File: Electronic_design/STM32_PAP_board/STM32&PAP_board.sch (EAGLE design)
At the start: 21 parts

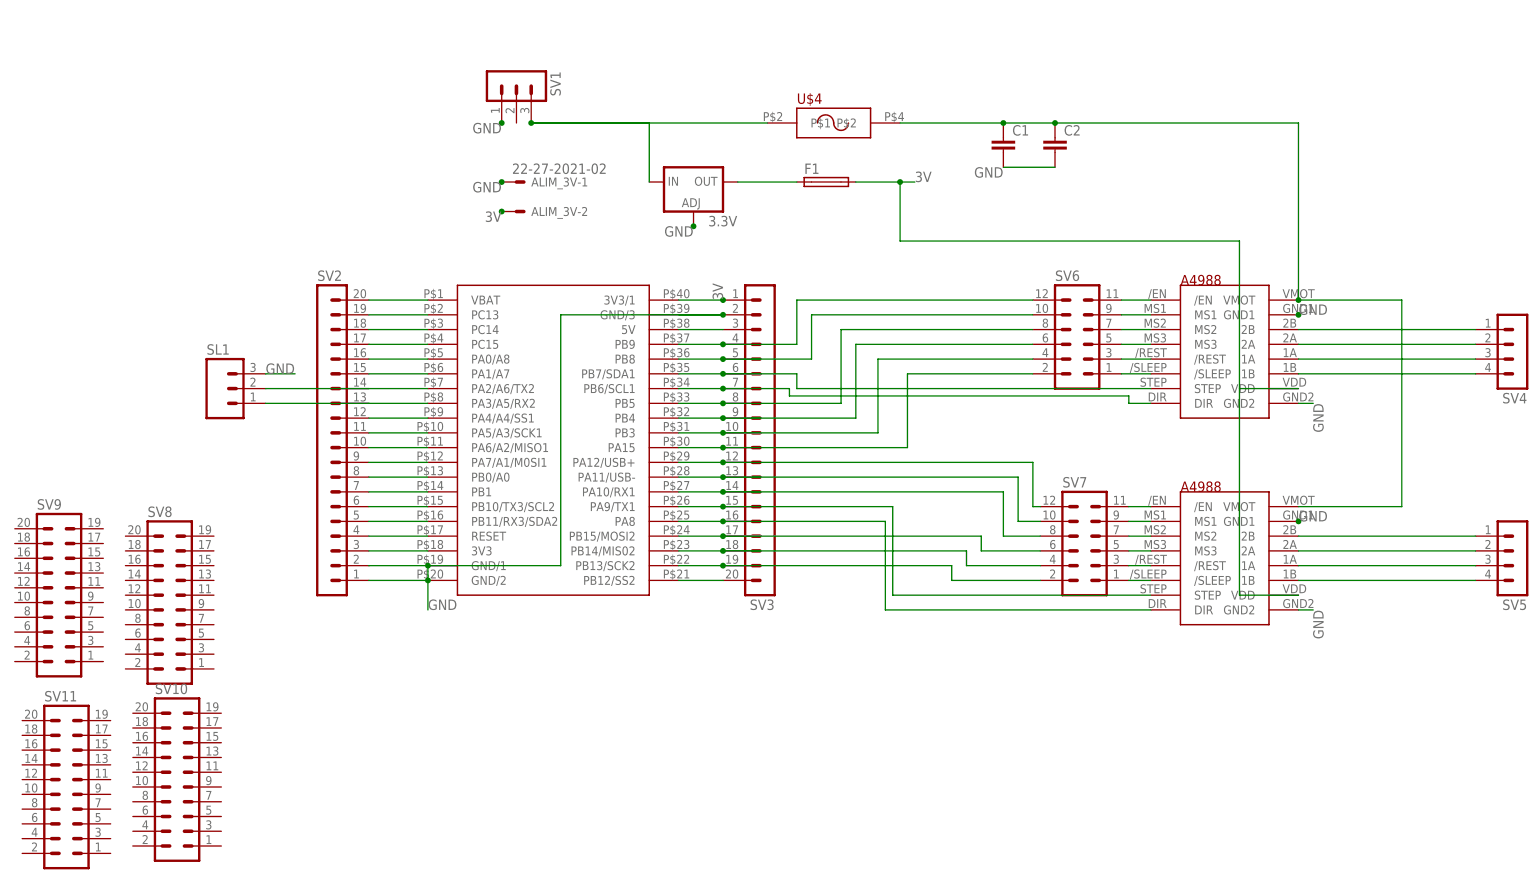
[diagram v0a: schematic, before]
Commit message: modification regulateur 3V3
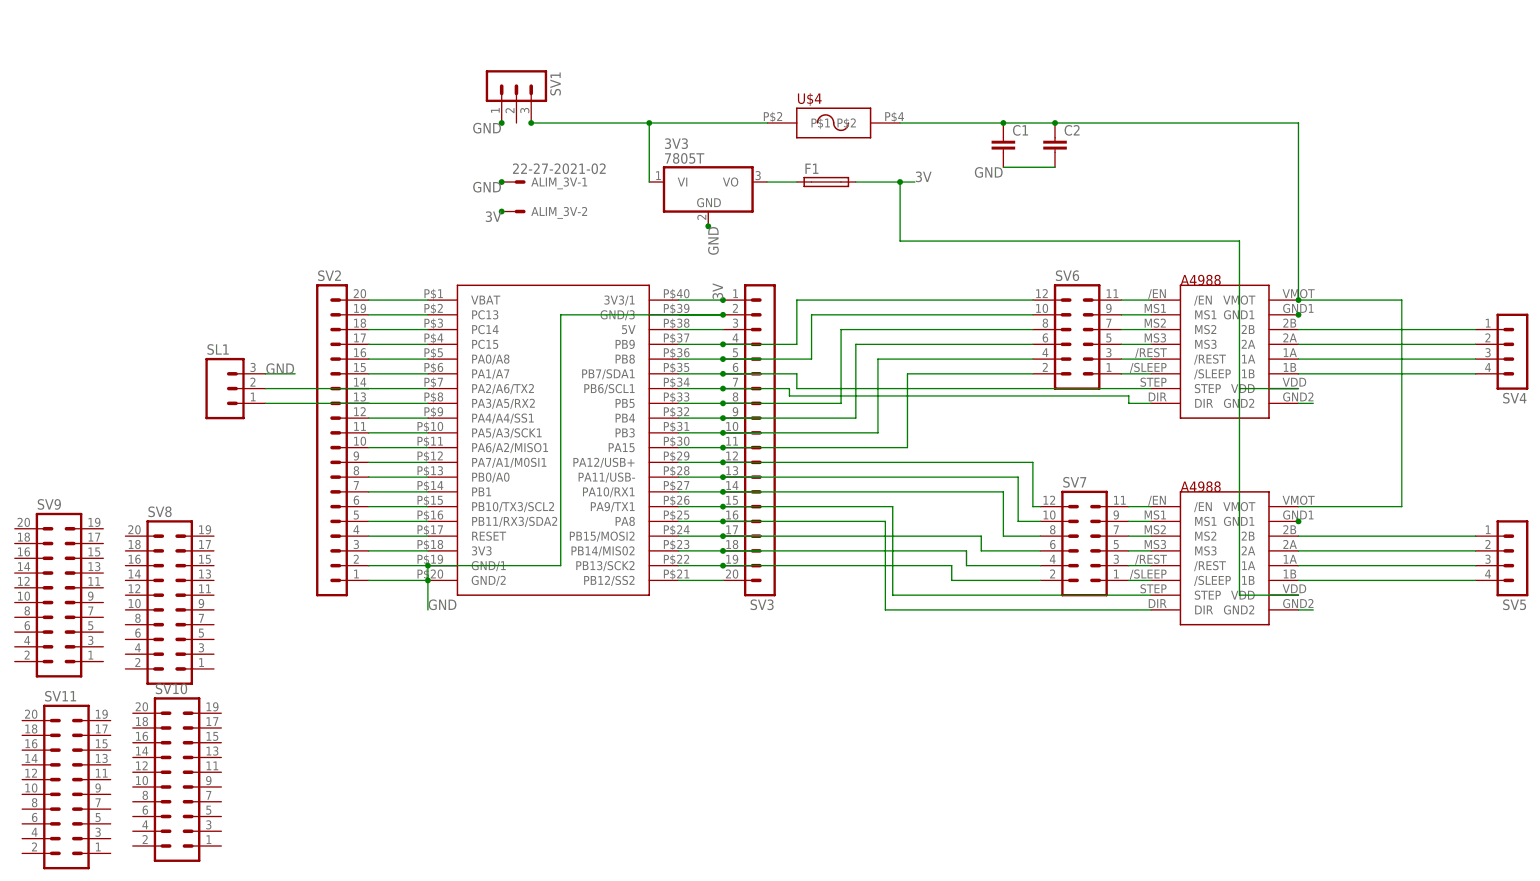
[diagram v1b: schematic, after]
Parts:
- removed 3.3V: (no value), v-reg:LM138-TS
- added 3V3: 7805T, linear:7805T
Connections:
- net GND: now also 3V3.GND; no longer 3.3V.ADJ
- net N$41: now also 3V3.VO; no longer 3.3V.OUT
- net N$42: now also 3V3.VI; no longer 3.3V.IN
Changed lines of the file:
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@@
 <part name="SV2" library="con-lstb" deviceset="MA20-1" device=""/>
 <part name="SV3" library="con-lstb" deviceset="MA20-1" device=""/>
-<part name="3.3V" library="v-reg" deviceset="LM138-TS" device=""/>
 <part name="SV4" library="con-lstb" deviceset="MA04-1" device=""/>
 <part name="SV5" library="con-lstb" deviceset="MA04-1" device=""/>
@@
 <part name="F1" library="fuse" deviceset="TR5" device=""/>
 <part name="SL1" library="con-amp-quick" deviceset="MA03" device=""/>
+<part name="3V3" library="linear" library_urn="urn:adsk.eagle:library:262" deviceset="78*" device="T" package3d_urn="urn:adsk.eagle:package:16414/1" technology="05"/>
 </parts>
 <sheets>
@@
 <instance part="SV2" gate="1" x="-81.28" y="5.08"/>
 <instance part="SV3" gate="1" x="-5.08" y="7.62" rot="R180"/>
-<instance part="3.3V" gate="G$1" x="-17.78" y="50.8"/>
 <instance part="SV4" gate="1" x="124.46" y="20.32" rot="R180"/>
 <instance part="SV5" gate="1" x="124.46" y="-15.24" rot="R180"/>
@@
 <instance part="F1" gate="1" x="5.08" y="50.8"/>
 <instance part="SL1" gate="G$1" x="-99.06" y="15.24"/>
+<instance part="3V3" gate="A1" x="-15.24" y="50.8"/>
 </instances>
 <busses>
@@
 </net>
 <net name="GND" class="0">
-<segment>
-<pinref part="3.3V" gate="G$1" pin="ADJ"/>
-<junction x="-17.78" y="43.18"/>
-<label x="-17.78" y="43.18" size="1.778" layer="95" rot="R180"/>
-<label x="86.36" y="27.94" size="1.778" layer="95"/>
-<label x="86.36" y="-7.62" size="1.778" layer="95"/>
-<label x="88.9" y="12.7" size="1.778" layer="95" rot="R270"/>
-<label x="88.9" y="-22.86" size="1.778" layer="95" rot="R270"/>
-</segment>
 <segment>
 <pinref part="U$3" gate="G$1" pin="GND/1"/>
@@
 <label x="-91.44" y="17.78" size="1.778" layer="95"/>
 </segment>
+<segment>
+<pinref part="3V3" gate="A1" pin="GND"/>
+<junction x="-15.24" y="43.18"/>
+<label x="-15.24" y="43.18" size="1.778" layer="95" rot="R270"/>
+</segment>
 </net>
 <net name="N$43" class="0">
@@
 </segment>
 </net>
-<net name="N$41" class="0">
-<segment>
-<pinref part="3.3V" gate="G$1" pin="OUT"/>
-<pinref part="F1" gate="1" pin="1"/>
-<wire x1="-10.16" y1="50.8" x2="0" y2="50.8" width="0.1524" layer="91"/>
-</segment>
-</net>
 <net name="N$42" class="0">
 <segment>
 <pinref part="U$4" gate="G$1" pin="P$1"/>
 <pinref part="SV1" gate="G$1" pin="3"/>
-<wire x1="-5.08" y1="60.96" x2="-45.72" y2="60.96" width="0.1524" layer="91"/>
-<pinref part="3.3V" gate="G$1" pin="IN"/>
-<wire x1="-25.4" y1="50.8" x2="-25.4" y2="60.96" width="0.1524" layer="91"/>
+<wire x1="-5.08" y1="60.96" x2="-25.4" y2="60.96" width="0.1524" layer="91"/>
 <wire x1="-25.4" y1="60.96" x2="-45.72" y2="60.96" width="0.1524" layer="91"/>
 <junction x="-45.72" y="60.96"/>
+<pinref part="3V3" gate="A1" pin="VI"/>
+<wire x1="-25.4" y1="50.8" x2="-25.4" y2="60.96" width="0.1524" layer="91"/>
+<junction x="-25.4" y="60.96"/>
 </segment>
 </net>
@@
 </segment>
 </net>
+<net name="N$41" class="0">
+<segment>
+<pinref part="3V3" gate="A1" pin="VO"/>
+<pinref part="F1" gate="1" pin="1"/>
+<wire x1="-5.08" y1="50.8" x2="0" y2="50.8" width="0.1524" layer="91"/>
+</segment>
+</net>
 </nets>
 </sheet>
@@
 </schematic>
 </drawing>
+<compatibility>
+<note version="8.2" severity="warning">
+Since Version 8.2, EAGLE supports online libraries. The ids
+of those online libraries will not be understood (or retained)
+with this version.
+</note>
+<note version="8.3" severity="warning">
+Since Version 8.3, EAGLE supports URNs for individual library
+assets (packages, symbols, and devices). The URNs of those assets
+will not be understood (or retained) with this version.
+</note>
+<note version="8.3" severity="warning">
+Since Version 8.3, EAGLE supports the association of 3D packages
+with devices in libraries, schematics, and board files. Those 3D
+packages will not be understood (or retained) with this version.
+</note>
+</compatibility>
 </eagle>

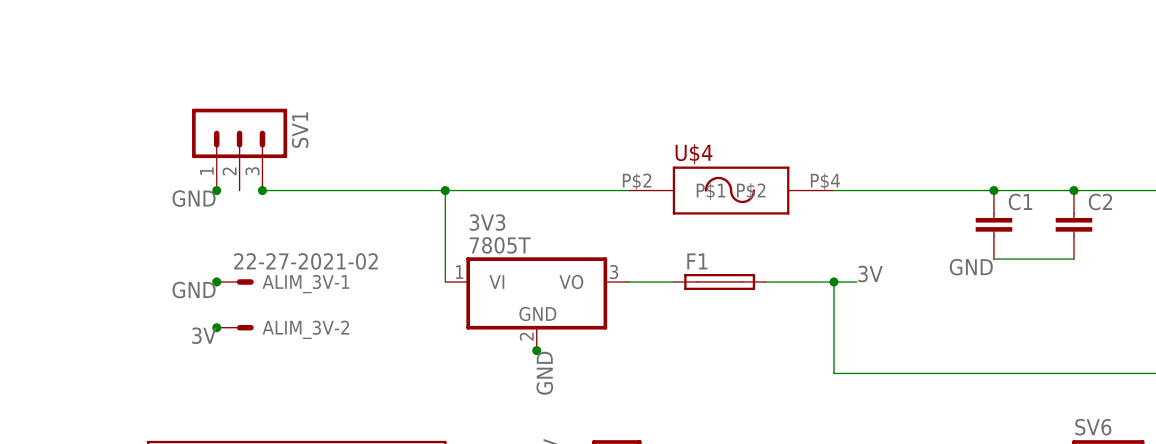
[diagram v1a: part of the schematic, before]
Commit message: ajout connecteur vert et trous de fixation
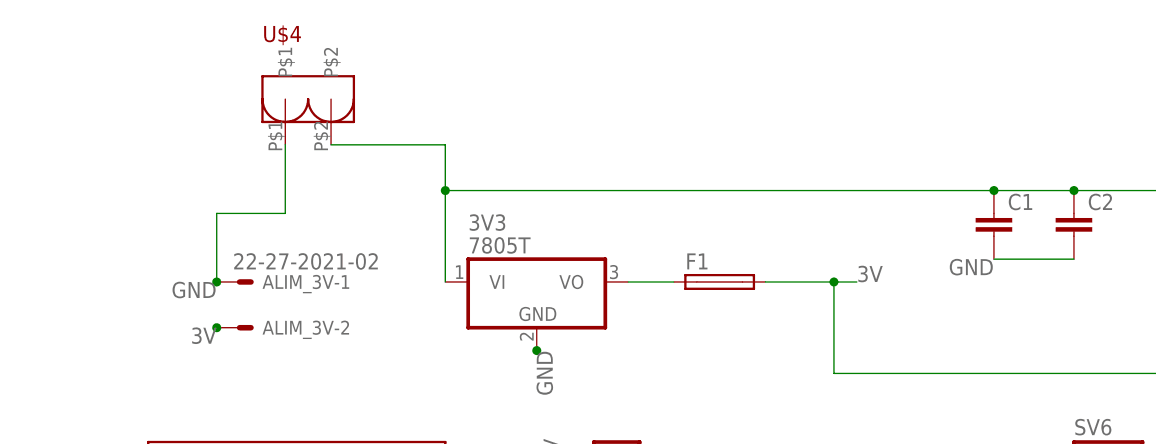
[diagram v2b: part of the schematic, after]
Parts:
- removed SV1: (no value), con-lstb:MA03-1
- U$4: value AUTO_FUSE -> GREEN_HEADER; device AUTO_FUSE:AUTO_FUSE -> PowerHeaders:GREEN_HEADER
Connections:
- removed net N$43: C1.1, C2.1, U$1.VMOT, U$2.VMOT, U$4.P$2
- net GND: now also U$4.P$1; no longer SV1.1
- net N$42: now also C1.1, C2.1, U$1.VMOT, U$2.VMOT, U$4.P$2; no longer SV1.3, U$4.P$1
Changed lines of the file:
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@@
 <part name="U$2" library="POLOLU_A4988_MOTOR_DRIVER" deviceset="POLOLU_A4988_MOTOR_DRIVER" device=""/>
 <part name="U$3" library="stm32duino boards" deviceset="BLUEPILL" device=""/>
-<part name="U$4" library="AUTO_FUSE" deviceset="AUTO_FUSE" device=""/>
-<part name="SV1" library="con-lstb" deviceset="MA03-1" device=""/>
 <part name="SV2" library="con-lstb" deviceset="MA20-1" device=""/>
 <part name="SV3" library="con-lstb" deviceset="MA20-1" device=""/>
@@
 <part name="SL1" library="con-amp-quick" deviceset="MA03" device=""/>
 <part name="3V3" library="linear" library_urn="urn:adsk.eagle:library:262" deviceset="78*" device="T" package3d_urn="urn:adsk.eagle:package:16414/1" technology="05"/>
+<part name="U$4" library="PowerHeaders" deviceset="GREEN_HEADER" device=""/>
 </parts>
 <sheets>
@@
 <instance part="U$2" gate="G$1" x="73.66" y="-12.7"/>
 <instance part="U$3" gate="G$1" x="-43.18" y="5.08"/>
-<instance part="U$4" gate="G$1" x="5.08" y="60.96"/>
-<instance part="SV1" gate="G$1" x="-48.26" y="68.58" rot="R270"/>
 <instance part="SV2" gate="1" x="-81.28" y="5.08"/>
 <instance part="SV3" gate="1" x="-5.08" y="7.62" rot="R180"/>
@@
 <instance part="SL1" gate="G$1" x="-99.06" y="15.24"/>
 <instance part="3V3" gate="A1" x="-15.24" y="50.8"/>
+<instance part="U$4" gate="G$1" x="-40.64" y="71.12"/>
 </instances>
 <busses>
@@
 </segment>
 <segment>
-<pinref part="SV1" gate="G$1" pin="1"/>
-<junction x="-50.8" y="60.96"/>
-<label x="-50.8" y="60.96" size="1.778" layer="95" rot="R180"/>
-</segment>
-<segment>
 <pinref part="ALIM_3V" gate="-1" pin="S"/>
 <junction x="-50.8" y="50.8"/>
 <label x="-50.8" y="50.8" size="1.778" layer="95" rot="R180"/>
+<pinref part="U$4" gate="G$1" pin="P$1"/>
+<wire x1="-43.18" y1="66.04" x2="-43.18" y2="58.42" width="0.1524" layer="91"/>
+<wire x1="-43.18" y1="58.42" x2="-50.8" y2="58.42" width="0.1524" layer="91"/>
+<wire x1="-50.8" y1="58.42" x2="-50.8" y2="50.8" width="0.1524" layer="91"/>
 </segment>
 <segment>
@@
 </segment>
 </net>
-<net name="N$43" class="0">
-<segment>
-<pinref part="U$4" gate="G$1" pin="P$2"/>
+<net name="N$45" class="0">
+<segment>
+<pinref part="U$1" gate="G$1" pin="GND1"/>
+<junction x="86.36" y="27.94"/>
+</segment>
+</net>
+<net name="N$46" class="0">
+<segment>
+<pinref part="U$2" gate="G$1" pin="GND1"/>
+<junction x="86.36" y="-7.62"/>
+</segment>
+</net>
+<net name="N$42" class="0">
+<segment>
+<pinref part="3V3" gate="A1" pin="VI"/>
+<wire x1="-25.4" y1="50.8" x2="-25.4" y2="60.96" width="0.1524" layer="91"/>
 <pinref part="U$1" gate="G$1" pin="VMOT"/>
-<wire x1="17.78" y1="60.96" x2="35.56" y2="60.96" width="0.1524" layer="91"/>
 <wire x1="35.56" y1="60.96" x2="44.45" y2="60.96" width="0.1524" layer="91"/>
 <wire x1="44.45" y1="60.96" x2="86.36" y2="60.96" width="0.1524" layer="91"/>
@@
 <pinref part="C2" gate="G$1" pin="1"/>
 <junction x="44.45" y="60.96"/>
-</segment>
-</net>
-<net name="N$45" class="0">
-<segment>
-<pinref part="U$1" gate="G$1" pin="GND1"/>
-<junction x="86.36" y="27.94"/>
-</segment>
-</net>
-<net name="N$46" class="0">
-<segment>
-<pinref part="U$2" gate="G$1" pin="GND1"/>
-<junction x="86.36" y="-7.62"/>
-</segment>
-</net>
-<net name="N$42" class="0">
-<segment>
-<pinref part="U$4" gate="G$1" pin="P$1"/>
-<pinref part="SV1" gate="G$1" pin="3"/>
-<wire x1="-5.08" y1="60.96" x2="-25.4" y2="60.96" width="0.1524" layer="91"/>
-<wire x1="-25.4" y1="60.96" x2="-45.72" y2="60.96" width="0.1524" layer="91"/>
-<junction x="-45.72" y="60.96"/>
-<pinref part="3V3" gate="A1" pin="VI"/>
-<wire x1="-25.4" y1="50.8" x2="-25.4" y2="60.96" width="0.1524" layer="91"/>
+<wire x1="-25.4" y1="60.96" x2="35.56" y2="60.96" width="0.1524" layer="91"/>
+<pinref part="U$4" gate="G$1" pin="P$2"/>
+<wire x1="-38.1" y1="66.04" x2="-25.4" y2="66.04" width="0.1524" layer="91"/>
+<wire x1="-25.4" y1="66.04" x2="-25.4" y2="60.96" width="0.1524" layer="91"/>
 <junction x="-25.4" y="60.96"/>
 </segment>

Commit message: ameliorations
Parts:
- removed SL1: (no value), con-amp-quick:MA03
- added SV1: (no value), con-lstb:MA10-1
- added UART2: (no value), con-amp-quick:MA03
- SV2: device con-lstb:MA20-1 -> con-lstb:MA08-1
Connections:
- net GND: now also UART2.3; no longer SL1.3, SV2.1, SV2.2
- net N$10: now also SV2.8; no longer SV2.10
- net N$11: now also SV1.1; no longer SV2.11
- net N$12: now also SV1.2; no longer SV2.12
- net N$13: now also SV1.3, UART2.2; no longer SL1.1, SV2.13
- net N$14: now also SV1.4, UART2.1; no longer SL1.2, SV2.14
- net N$15: now also SV1.5; no longer SV2.15
- net N$16: now also SV1.6; no longer SV2.16
- net N$17: now also SV1.7; no longer SV2.17
- net N$18: now also SV1.8; no longer SV2.18
- net N$19: now also SV1.9; no longer SV2.19
- net N$20: now also SV1.10; no longer SV2.20
- net N$3: now also SV2.1; no longer SV2.3
- net N$4: now also SV2.2; no longer SV2.4
- net N$5: now also SV2.3; no longer SV2.5
- net N$6: now also SV2.4; no longer SV2.6
- net N$7: now also SV2.5; no longer SV2.7
- net N$8: now also SV2.6; no longer SV2.8
- net N$9: now also SV2.7; no longer SV2.9

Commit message: ajout condensateurs
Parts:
- added C3: (no value), rcl:CPOL-EUE5-13
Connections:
- net GND: now also C3.-
- net N$42: now also C3.+
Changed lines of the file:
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@@
 <part name="SV1" library="con-lstb" library_urn="urn:adsk.eagle:library:162" deviceset="MA10-1" device="" package3d_urn="urn:adsk.eagle:package:8346/1"/>
 <part name="SV2" library="con-lstb" library_urn="urn:adsk.eagle:library:162" deviceset="MA08-1" device="" package3d_urn="urn:adsk.eagle:package:8343/1"/>
+<part name="C3" library="rcl" library_urn="urn:adsk.eagle:library:334" deviceset="CPOL-EU" device="E5-13" package3d_urn="urn:adsk.eagle:package:23375/1"/>
 </parts>
 <sheets>
@@
 <instance part="SV1" gate="1" x="-93.98" y="17.78"/>
 <instance part="SV2" gate="1" x="-93.98" y="-5.08"/>
+<instance part="C3" gate="G$1" x="-33.02" y="63.5"/>
 </instances>
 <busses>
@@
 <junction x="-15.24" y="43.18"/>
 <label x="-15.24" y="43.18" size="1.778" layer="95" rot="R270"/>
+<pinref part="C3" gate="G$1" pin="-"/>
+<wire x1="-33.02" y1="58.42" x2="-33.02" y2="43.18" width="0.1524" layer="91"/>
+<wire x1="-33.02" y1="43.18" x2="-15.24" y2="43.18" width="0.1524" layer="91"/>
 </segment>
 <segment>
@@
 <wire x1="-25.4" y1="60.96" x2="35.56" y2="60.96" width="0.1524" layer="91"/>
 <pinref part="U$4" gate="G$1" pin="P$2"/>
-<wire x1="-38.1" y1="66.04" x2="-25.4" y2="66.04" width="0.1524" layer="91"/>
+<wire x1="-38.1" y1="66.04" x2="-33.02" y2="66.04" width="0.1524" layer="91"/>
+<wire x1="-33.02" y1="66.04" x2="-25.4" y2="66.04" width="0.1524" layer="91"/>
 <wire x1="-25.4" y1="66.04" x2="-25.4" y2="60.96" width="0.1524" layer="91"/>
 <junction x="-25.4" y="60.96"/>
-</segment>
-</net>
+<pinref part="C3" gate="G$1" pin="+"/>
+<junction x="-33.02" y="66.04"/>
+</segment>
+</net>
